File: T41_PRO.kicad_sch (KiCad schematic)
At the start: 0 parts

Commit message: Finished IMX1062 symbol
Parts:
- added U1: ~, symbol local:MIMXRT1062DVJ6B

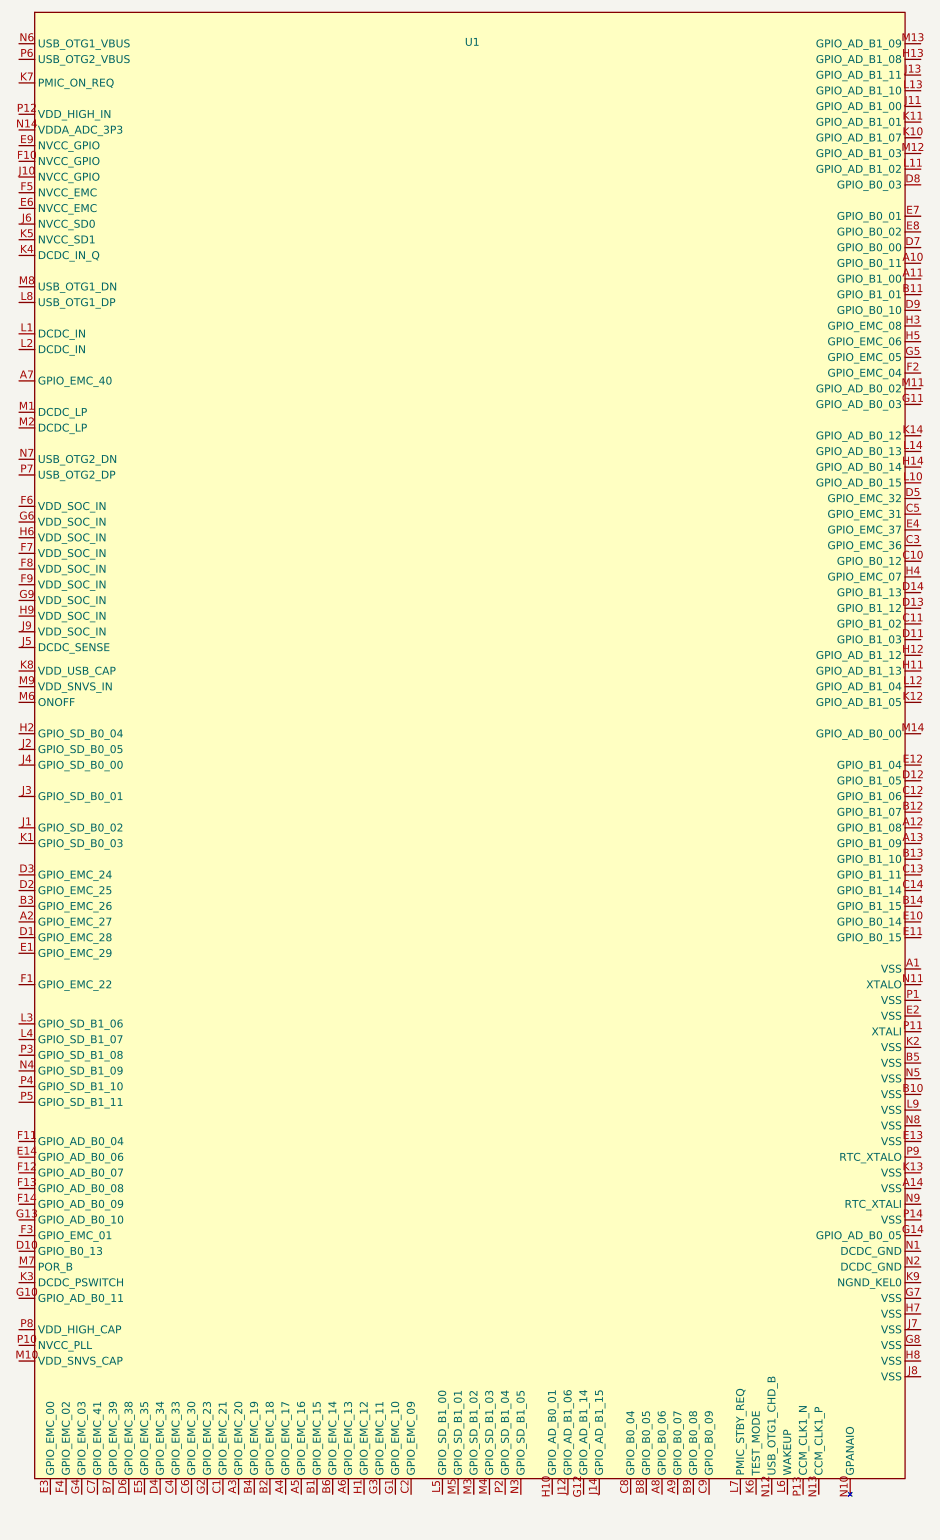
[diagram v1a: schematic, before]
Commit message: No Gaps in 1062 sym
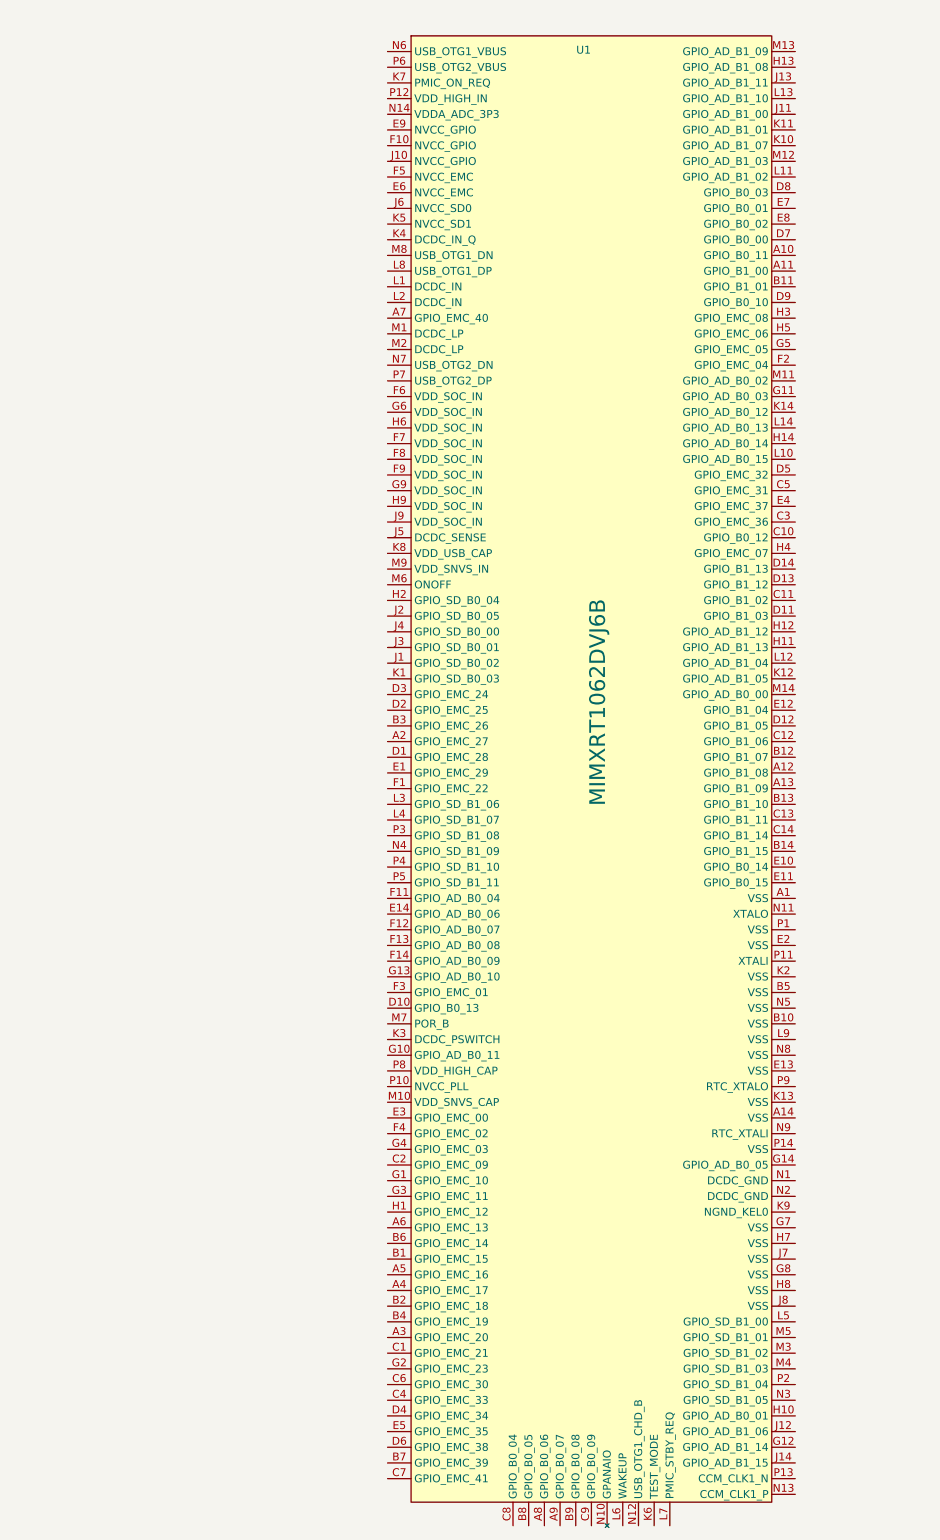
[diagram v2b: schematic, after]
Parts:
- U1: value ~ -> MIMXRT1062DVJ6B
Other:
- company: (none) -> David Asmuth
- title: (none) -> T41_PRO
- moved on the sheet: U1
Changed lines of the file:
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@@
 	(generator_version "9.0")
 	(paper "A3")
+	(title_block
+		(title "T41_PRO")
+		(date "2025-07-19")
+		(rev "0")
+		(company "David Asmuth")
+		(comment 1 "Teensy compatible production read module")
+	)
 	(symbol
 		(lib_id "local:MIMXRT1062DVJ6B")
-		(at 143.51 15.24 0)
+		(at 204.47 19.05 0)
 		(unit 1)
 		(exclude_from_sim no)
@@
 		(dnp no)
 		(property "Reference" "U1"
-			(at 190.246 20.066 0)
+			(at 208.28 21.336 0)
 			(effects
 				(font
@@
 			)
 		)
-		(property "Value" "~"
-			(at 176.53 8.89 0)
+		(property "Value" "MIMXRT1062DVJ6B"
+			(at 210.566 127 90)
 			(effects
 				(font
-					(size 1.27 1.27)
+					(size 2.54 2.54)
 				)
 			)
 		)
 		(property "Footprint" ""
-			(at 143.51 15.24 0)
+			(at 204.47 19.05 0)
 			(effects
 				(font
@@
 		)
 		(property "Datasheet" ""
-			(at 143.51 15.24 0)
+			(at 204.47 19.05 0)
 			(effects
 				(font
@@
 		)
 		(property "Description" ""
-			(at 143.51 15.24 0)
+			(at 204.47 19.05 0)
 			(effects
 				(font
